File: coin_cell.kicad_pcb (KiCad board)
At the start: 2 copper layers, 11 parts, among them J1 Barrel_Jack, U1 NC7SZ14-D, U2 TPS61222

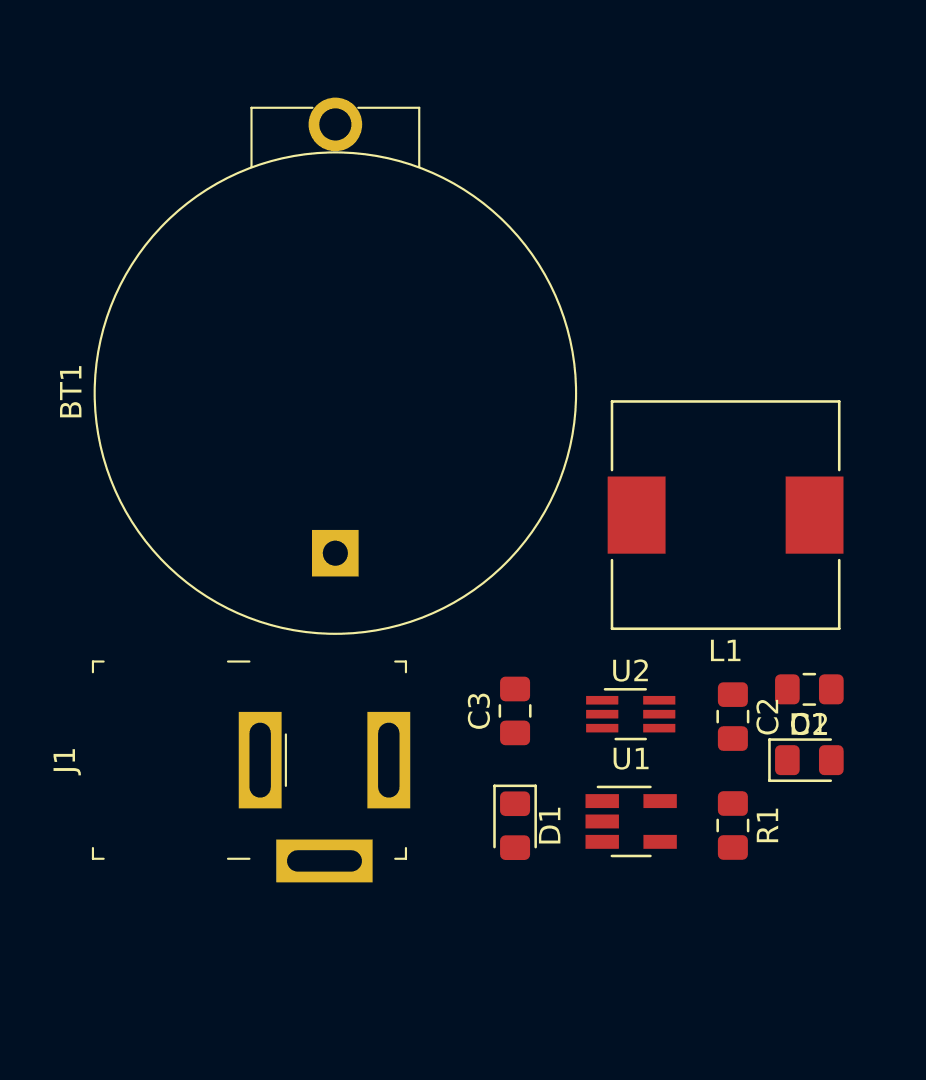
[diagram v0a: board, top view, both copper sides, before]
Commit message: pcbnew component placement
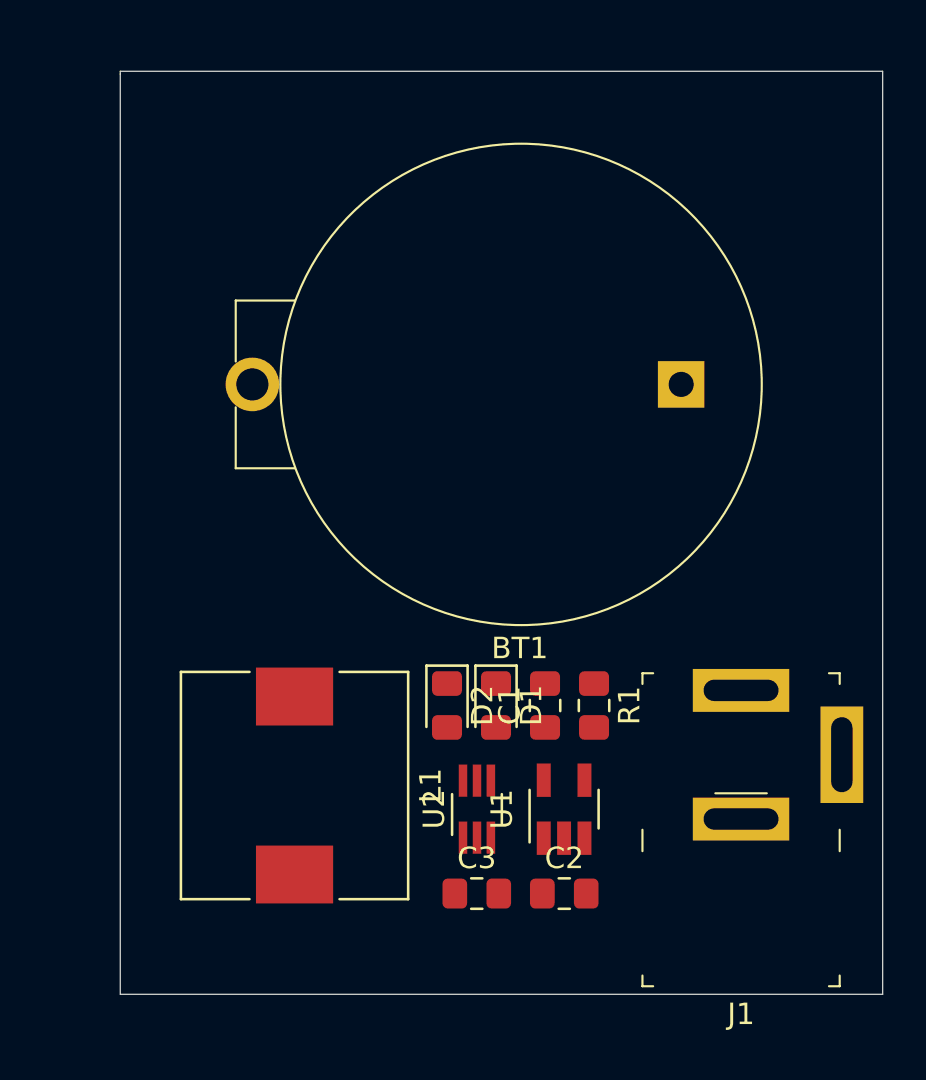
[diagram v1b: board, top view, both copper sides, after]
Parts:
- moved L1 23.7 mm to (24.5, 47.9), turned to 270 degrees
- moved J1 19.4 mm to (45.3, 46.5), turned to 180 degrees
- moved BT1 17.9 mm to (42.5, 29.2), turned to 180 degrees
- moved D2 17.1 mm to (31.6, 44.2), turned to 270 degrees
- moved C1 12.4 mm to (36.2, 44.2), turned to 90 degrees
- moved C2 11.4 mm to (37.1, 53.0), turned to 0 degrees
- moved C3 8.70 mm to (33.0, 53.0), turned to 0 degrees
- moved R1 8.56 mm to (38.5, 44.2)
- moved U2 8.43 mm to (33.0, 49.0), turned to 90 degrees
- moved D1 5.68 mm to (33.9, 44.2)
- moved U1 3.18 mm to (37.1, 49.0), turned to 90 degrees
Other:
- board outline added: 35.6 x 43.1 mm

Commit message: Added reference pcb layout
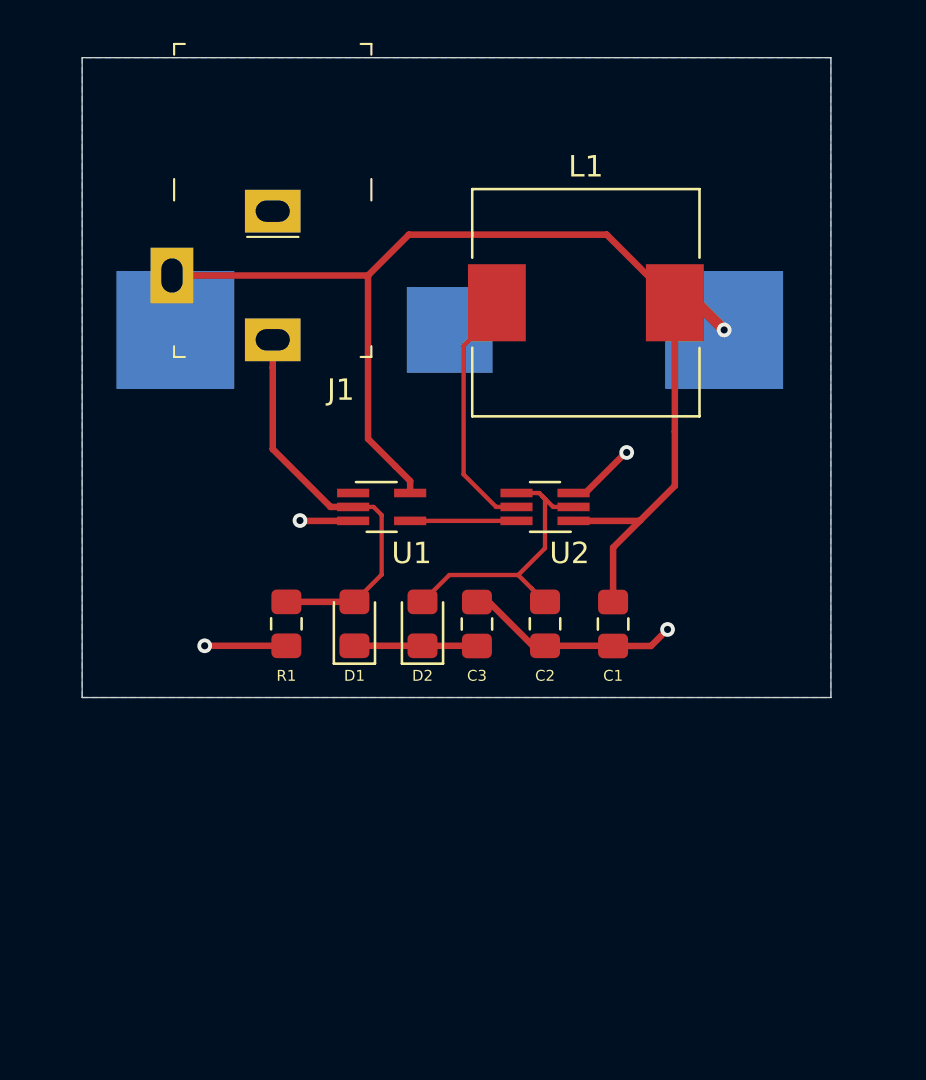
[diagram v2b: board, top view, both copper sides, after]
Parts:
- BT1: footprint digikey-footprints:Battery_Holder_Coin_2032_BS-7 -> coin_cell:S8211R; moved to B.Cu
- C1, C2, C3: footprint Capacitor_SMD:C_0805_2012Metric_Pad1.15x1.40mm_HandSolder -> coin_cell:Capacitor_0805_2012Metric_Pad1.15x1.40mm_HandSolder
- D1, D2: footprint Diode_SMD:D_0805_2012Metric_Pad1.15x1.40mm_HandSolder -> coin_cell:Diode_0805_2012Metric_Pad1.15x1.40mm_HandSolder
- J1: footprint digikey-footprints:Barrel_Jack_5.5mmODx2.1mmID_PJ-202A -> coin_cell:Barrel_Jack_Small_Hole_Type_5.5mmODx2.1mmID_PJ-102A
- R1: footprint Resistor_SMD:R_0805_2012Metric_Pad1.15x1.40mm_HandSolder -> coin_cell:Resistor_0805_2012Metric_Pad1.15x1.40mm_HandSolder
- U1: footprint coin_cell:SOT-23-5_HandSoldering -> coin_cell:SOT-353_SC-70-5_Handsoldering
- U2: footprint Package_TO_SOT_SMD:SOT-363_SC-70-6_Handsoldering -> coin_cell:SOT-363_SC-70-6_Handsoldering
- moved J1 31.3 mm to (23.5, 24.1), turned to 0 degrees
- moved L1 26.3 mm to (38.1, 25.4), turned to 0 degrees
- moved U1 16.5 mm to (28.6, 34.9), turned to 0 degrees
- moved R1 14.8 mm to (24.1, 40.4), turned to 90 degrees
- moved U2 14.5 mm to (36.2, 34.9), turned to 180 degrees
- moved C2 12.6 mm to (36.2, 40.4), turned to 270 degrees
- moved C3 12.6 mm to (33.0, 40.4), turned to 90 degrees
- moved BT1 11.1 mm to (31.8, 26.7)
- moved D1 7.62 mm to (27.3, 40.4), turned to 90 degrees
- moved C1 4.95 mm to (39.4, 40.4), turned to 270 degrees
- moved D2 3.98 mm to (30.5, 40.4), turned to 90 degrees
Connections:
- J1 pad 3: (no net) -> V_BATT
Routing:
- net V_BATT: track 0.00 -> 57.6 mm, vias 0 -> 1
- net GND: track 0.00 -> 19.6 mm, vias 0 -> 4
- net 5V_WALL: track 0.00 -> 19.2 mm
- net Net-(C2-Pad1): track 0.00 -> 13.9 mm
- net Net-(L1-Pad1): track 0.00 -> 11.7 mm
- net 5V_SHARED: track 0.00 -> 5.72 mm
- net EN: track 0.00 -> 4.96 mm
- added copper zone on B.Cu, net GND
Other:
- board size 35.6 x 43.1 mm -> 34.9 x 29.8 mm
- net class Default: clearance 0.2 -> 0.1524; trace_width 0.25 -> 0.3048; via_dia 0.8 -> 0.6858; via_drill 0.4 -> 0.3302
- rule pad_to_mask_clearance: 0.051 -> 0.00129
- rule solder_mask_min_width: 0.25 -> 0.002565
- rule trace_clearance: 0.2 -> 0.1524
- rule trace_min: 0.2 -> 0.1524
- rule via_min_drill: 0.3 -> 0.254
- rule via_min_size: 0.4 -> 0.508

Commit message: Adjusted clearances and trace widths
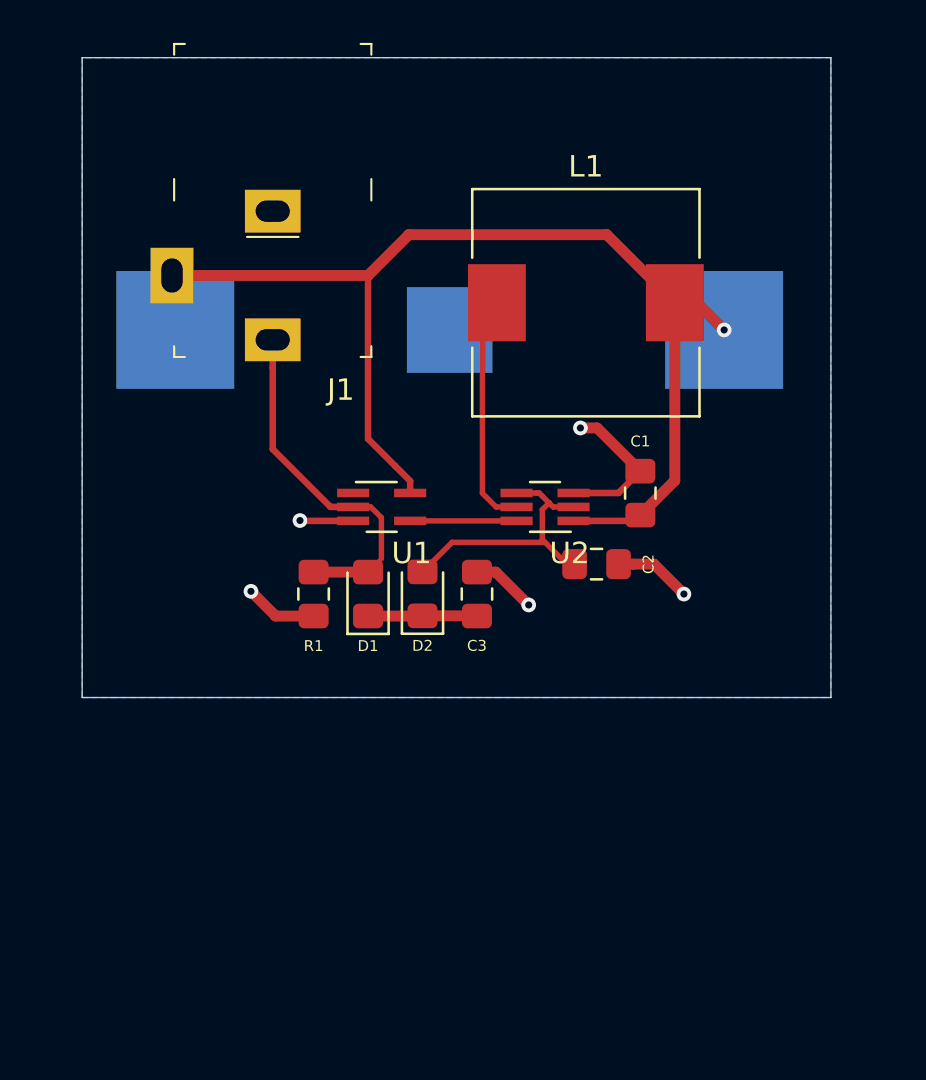
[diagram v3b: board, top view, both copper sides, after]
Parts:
- moved C1 6.24 mm to (40.6, 34.3), turned to 90 degrees
- moved C2 3.68 mm to (38.6, 37.6), turned to 0 degrees
- moved R1 1.88 mm to (25.4, 39.0)
- moved D1 1.53 mm to (27.9, 39.0)
- moved C3 1.40 mm to (33.0, 39.0)
- moved D2 1.40 mm to (30.5, 39.0)
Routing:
- net V_BATT: track 57.6 -> 53.1 mm
- net 5V_WALL: track 19.2 -> 16.8 mm
- net Net-(C2-Pad1): track 13.9 -> 13.0 mm
- net Net-(L1-Pad1): track 11.7 -> 11.0 mm
- net 5V_SHARED: track 5.72 -> 5.09 mm
- net GND: track 19.6 -> 19.7 mm, vias 4 -> 5
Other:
- net class Default: trace_width 0.3048 -> 0.254

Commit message: Moved component labels to improve readability
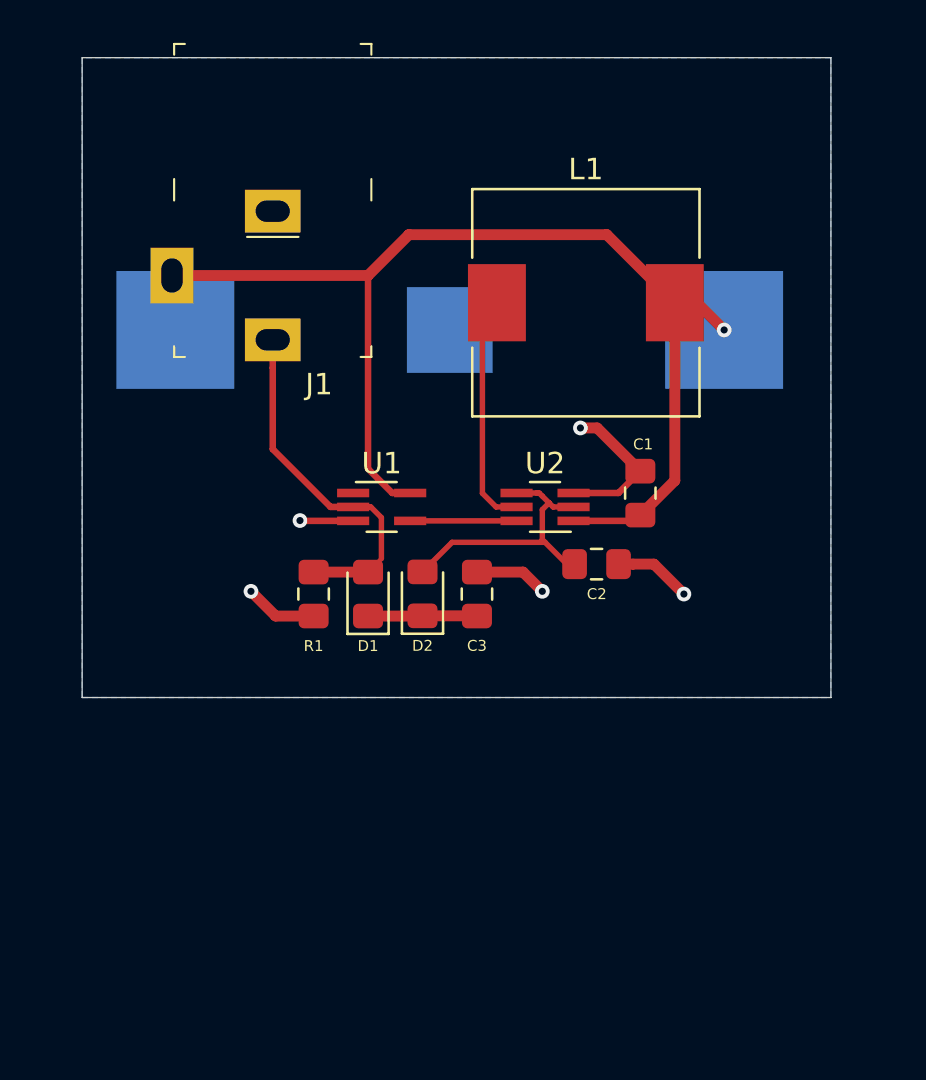
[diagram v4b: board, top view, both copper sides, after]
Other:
- net class Default: trace_width 0.254 -> 0.508
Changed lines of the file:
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@@
     (thickness 1.6)
     (drawings 4)
-    (tracks 65)
+    (tracks 64)
     (zones 0)
     (modules 11)
@@
   )
   (setup
-    (last_trace_width 0.254)
+    (last_trace_width 0.508)
     (trace_clearance 0.1524)
     (zone_clearance 0.508)
@@
   (net_class Default "This is the default net class."
     (clearance 0.1524)
-    (trace_width 0.254)
+    (trace_width 0.508)
     (via_dia 0.6858)
     (via_drill 0.3302)
@@
     (tags "capacitor handsolder")
     (attr smd)
-    (fp_text reference C2 (at 2.422 0 -90) (layer F.SilkS)
+    (fp_text reference C2 (at 0.009 1.397 180) (layer F.SilkS)
       (effects (font (size 0.508 0.508) (thickness 0.127)))
     )
@@
     (tags "capacitor handsolder")
     (attr smd)
-    (fp_text reference C1 (at 2.413 0 180) (layer F.SilkS)
+    (fp_text reference C1 (at 2.277 0.127 180) (layer F.SilkS)
       (effects (font (size 0.508 0.508) (thickness 0.127)))
     )
@@
   (module coin_cell:Barrel_Jack_Small_Hole_Type_5.5mmODx2.1mmID_PJ-102A (layer F.Cu)
     (at 23.495 24.13)
-    (fp_text reference J1 (at 3.175 5.334) (layer F.SilkS)
+    (fp_text reference J1 (at 2.159 5.08) (layer F.SilkS)
       (effects (font (size 1 1) (thickness 0.15)))
     )
@@
     (tags "Choke SMD")
     (attr smd)
-    (fp_text reference L1 (at 0 -6.35) (layer F.SilkS)
+    (fp_text reference L1 (at 0 -6.223) (layer F.SilkS)
       (effects (font (size 1 1) (thickness 0.15)))
     )
@@
     (tags "SOT-353 SC-70-5 Handsoldering")
     (attr smd)
-    (fp_text reference U1 (at 1.397 2.159) (layer F.SilkS)
+    (fp_text reference U1 (at 0 -2.032) (layer F.SilkS)
       (effects (font (size 1 1) (thickness 0.15)))
     )
@@
     (tags "SOT-363 SC-70-6 Handsoldering")
     (attr smd)
-    (fp_text reference U2 (at -1.143 -2.159) (layer F.SilkS)
+    (fp_text reference U2 (at 0 2.032) (layer F.SilkS)
       (effects (font (size 1 1) (thickness 0.15)))
     )
@@
   (gr_line (start 14.605 43.815) (end 49.53 43.815) (layer Edge.Cuts) (width 0.05))
   (gr_line (start 14.605 13.97) (end 14.605 43.815) (layer Edge.Cuts) (width 0.05))
-  (segment (start 29.905 34.275) (end 29.905 33.715) (width 0.3048) (layer F.Cu) (net 1))
-  (segment (start 29.905 33.715) (end 29.21 33.02) (width 0.3048) (layer F.Cu) (net 1))
-  (segment (start 29.21 33.02) (end 27.94 31.75) (width 0.3048) (layer F.Cu) (net 1))
   (via (at 44.55 26.67) (size 0.6858) (drill 0.3302) (layers F.Cu B.Cu) (net 1))
   (segment (start 42.25 25.4) (end 43.28 25.4) (width 0.508) (layer F.Cu) (net 1))
@@
   (segment (start 39.075 22.225) (end 42.25 25.4) (width 0.508) (layer F.Cu) (net 1))
   (segment (start 29.845 22.225) (end 39.075 22.225) (width 0.508) (layer F.Cu) (net 1))
-  (segment (start 27.94 31.75) (end 27.94 24.13) (width 0.3048) (layer F.Cu) (net 1))
   (segment (start 27.94 24.13) (end 29.845 22.225) (width 0.508) (layer F.Cu) (net 1))
   (segment (start 27.94 24.13) (end 18.795 24.13) (width 0.508) (layer F.Cu) (net 1))
@@
   (segment (start 42.25 33.696) (end 42.25 25.4) (width 0.508) (layer F.Cu) (net 1))
   (segment (start 40.64 35.306) (end 42.25 33.696) (width 0.508) (layer F.Cu) (net 1))
+  (segment (start 27.94 33.147) (end 27.94 24.13) (width 0.3048) (layer F.Cu) (net 1))
+  (segment (start 29.905 34.275) (end 29.068 34.275) (width 0.3048) (layer F.Cu) (net 1))
+  (segment (start 29.068 34.275) (end 27.94 33.147) (width 0.3048) (layer F.Cu) (net 1))
   (via (at 24.765 35.56) (size 0.6858) (drill 0.3302) (layers F.Cu B.Cu) (net 2))
   (segment (start 27.245 35.575) (end 24.78 35.575) (width 0.3048) (layer F.Cu) (net 2))
@@
   (segment (start 40.64 33.256) (end 38.626 31.242) (width 0.508) (layer F.Cu) (net 2))
   (segment (start 38.626 31.242) (end 37.846 31.242) (width 0.508) (layer F.Cu) (net 2))
-  (via (at 35.433 39.497) (size 0.6858) (drill 0.3302) (layers F.Cu B.Cu) (net 2))
-  (segment (start 33.02 37.964) (end 33.9 37.964) (width 0.508) (layer F.Cu) (net 2))
-  (segment (start 33.9 37.964) (end 35.433 39.497) (width 0.508) (layer F.Cu) (net 2))
   (via (at 22.479 38.862) (size 0.6858) (drill 0.3302) (layers F.Cu B.Cu) (net 2))
   (segment (start 25.4 40.014) (end 23.631 40.014) (width 0.508) (layer F.Cu) (net 2))
@@
   (segment (start 40.299 37.592) (end 41.275 37.592) (width 0.508) (layer F.Cu) (net 2))
   (segment (start 41.275 37.592) (end 42.672 38.989) (width 0.508) (layer F.Cu) (net 2))
+  (via (at 36.068 38.862) (size 0.6858) (drill 0.3302) (layers F.Cu B.Cu) (net 2))
+  (segment (start 33.02 37.964) (end 35.17 37.964) (width 0.508) (layer F.Cu) (net 2))
+  (segment (start 35.17 37.964) (end 36.068 38.862) (width 0.508) (layer F.Cu) (net 2))
   (segment (start 35.8182 34.275) (end 34.865 34.275) (width 0.254) (layer F.Cu) (net 3))
   (segment (start 35.9218 34.275) (end 35.8182 34.275) (width 0.254) (layer F.Cu) (net 3))
